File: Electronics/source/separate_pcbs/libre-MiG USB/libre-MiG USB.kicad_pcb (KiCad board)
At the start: 2 copper layers, 20 x 20 mm, 11 parts, among them J5 Conn_01x05, P1 USB_C_Plug_USB2.0

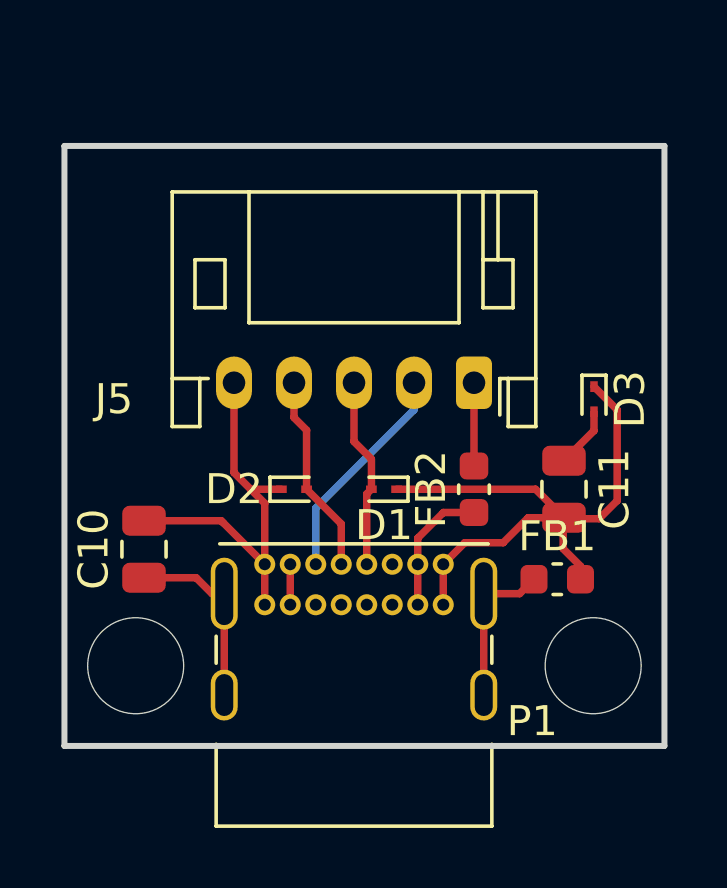
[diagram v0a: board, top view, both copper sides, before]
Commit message: added mechanical ignore
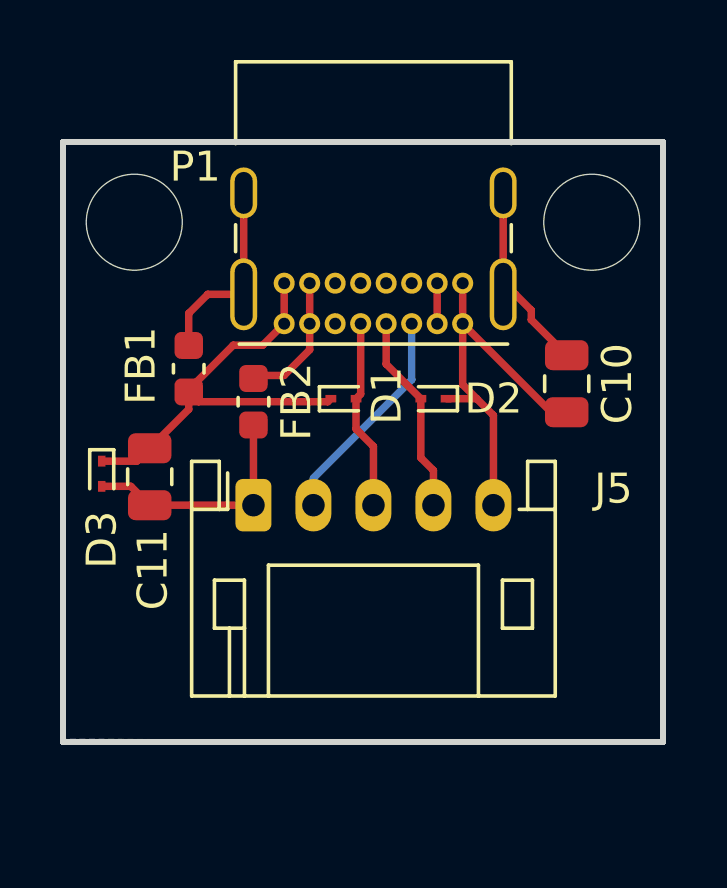
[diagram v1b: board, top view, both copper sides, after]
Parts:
- removed the REF** at (108.6, 187.7)
- removed the REF** at (123.8, 187.6)
- added REF**: MountingHole_3.2mm_M3, MountingHole:MountingHole_3.2mm_M3, F.Cu at (124.1, 172.6)
- added REF**: MountingHole_3.2mm_M3, MountingHole:MountingHole_3.2mm_M3, F.Cu at (108.9, 172.7)
- moved D3 16.6 mm to (107.6, 181.1)
- moved C10 15.1 mm to (123.1, 178.1), turned to -90 degrees
- moved FB1 14.1 mm to (110.5, 177.6), turned to -90 degrees
- moved C11 13.8 mm to (109.2, 181.2), turned to 90 degrees
- moved P1 10.4 mm to (119.6, 176.1), turned to 180 degrees
- moved J5 8.41 mm to (112.7, 182.2), turned to 0 degrees
- moved FB2 7.91 mm to (112.7, 178.7), turned to -90 degrees
- moved D2 5.54 mm to (118.7, 178.6), turned to 180 degrees
- moved D1 3.31 mm to (115.7, 178.6), turned to 0 degrees
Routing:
- net GND: track 33.9 -> 27.9 mm
- net +5V: track 4.82 -> 8.09 mm
- net Net-(C10-Pad1): track 11.5 -> 12.9 mm
- added copper zone on B.Cu, net GND

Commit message: Changed MCU to STM32F072 variant with built-in USB and removed wrong FTDI chip
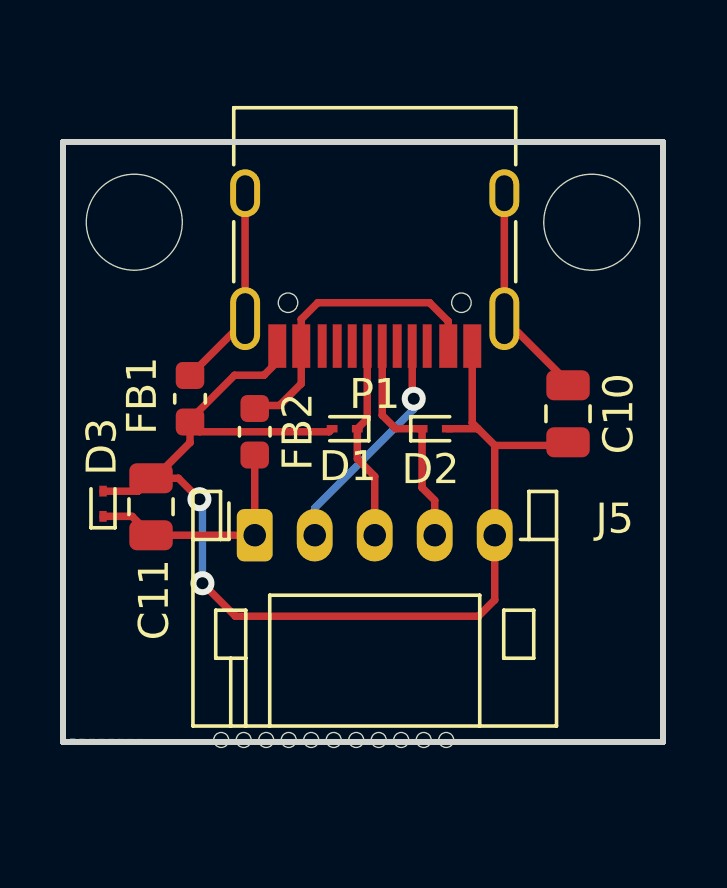
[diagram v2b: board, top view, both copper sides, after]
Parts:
- added ?: , , F.Cu at (111.6, 190.0)
- added ?: , , F.Cu at (117.6, 190.0)
- added ?: , , F.Cu at (113.8, 190.0)
- added ?: , , F.Cu at (118.3, 190.0)
- added ?: , , F.Cu at (113.1, 190.0)
- added ?: , , F.Cu at (112.3, 190.0)
- added ?: , , F.Cu at (116.8, 190.0)
- added ?: , , F.Cu at (115.3, 190.0)
- added ?: , , F.Cu at (119.1, 190.0)
- added ?: , , F.Cu at (116.1, 190.0)
- added ?: , , F.Cu at (114.6, 190.0)
- P1: footprint Connector_USB:USB_C_Receptacle_GCT_USB4085 -> Connector_USB:USB_C_Receptacle_HRO_TYPE-C-31-M-12
- moved P1 4.41 mm to (116.7, 172.8)
- moved C10 1.00 mm to (123.1, 179.2)
- moved D1 1.00 mm to (115.7, 179.6), turned to 180 degrees
- moved D2 1.00 mm to (118.7, 179.6), turned to 0 degrees
- moved D3 1.00 mm to (107.6, 182.2), turned to 90 degrees
- moved FB1 1.00 mm to (110.5, 178.7)
- moved FB2 1.00 mm to (112.7, 179.8)
- moved J5 1.00 mm to (112.7, 183.2)
- moved C11 1.00 mm to (109.2, 182.2)
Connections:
- D1 pad 1: GND -> (no net)
- D1 pad 2: Net-(D1-Pad2) -> GND
- D2 pad 1: GND -> (no net)
- D2 pad 2: Net-(D2-Pad2) -> GND
- D3 pad 1: GND -> +5V
- D3 pad 2: +5V -> GND
- J5 pad 3: Net-(D1-Pad2) -> (no net)
- J5 pad 4: Net-(D2-Pad2) -> (no net)
- P1 pad A6: Net-(D2-Pad2) -> (no net)
- P1 pad A7: Net-(D1-Pad2) -> (no net)
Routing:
- net (no net): track 0.00 -> 14.2 mm
- net GND: track 27.9 -> 41.2 mm, vias 0 -> 2
- net Net-(D2-Pad2): track 6.70 -> 0.00 mm
- net Net-(D1-Pad2): track 6.35 -> 0.00 mm
- net Net-(FB2-Pad1): track 5.80 -> 10.2 mm
- net Net-(C10-Pad1): track 12.9 -> 14.1 mm
- net Net-(J5-Pad2): track 7.41 -> 7.69 mm, vias 0 -> 1
